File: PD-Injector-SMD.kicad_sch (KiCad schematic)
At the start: 6 parts, among them P1 USB_C_Plug_USB2.0

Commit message: change of form factor and further ECAD work
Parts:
- removed H1: MountingHole, MountingHole:MountingHole_3.2mm_M3_Pad_Via, symbol Mechanical:MountingHole_Pad
- added D1: LED, LED_SMD:LED_0402_1005Metric, symbol Device:LED
- added H2: MountingHole, Eagle_WA-SMSI (rev21a):WA-SMSI_9774005243, symbol Mechanical:MountingHole_Pad
- added R3: 5.1k, Resistor_SMD:R_0402_1005Metric, symbol Device:R
- added TP1, TP2: TestPoint, TestPoint:TestPoint_Pad_D2.0mm, symbol Connector:TestPoint
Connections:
- net GND: now also D1.1 (K), H2.1, TP2.1
- net VBUS: now also TP1.1
- net at USB-C2.A4 (VBUS), USB-C2.B9 (VBUS): now also R3.1
- new net: D1.2 (A), R3.2
- no-connect marks 10 -> 9
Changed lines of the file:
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@@
   (junction (at 175.26 157.48) (diameter 0) (color 0 0 0 0)
   )
+  (junction (at 116.84 57.15) (diameter 0) (color 0 0 0 0)
+  )
   (junction (at 134.62 121.92) (diameter 0) (color 0 0 0 0)
   )
@@
   )
   (junction (at 116.84 134.62) (diameter 0) (color 0 0 0 0)
+  )
+  (junction (at 134.62 119.38) (diameter 0) (color 0 0 0 0)
   )
   (no_connect (at 114.3 69.85))
@@
   (no_connect (at 114.3 144.78))
   (no_connect (at 114.3 142.24))
-  (no_connect (at 114.3 114.3))
   (no_connect (at 83.82 114.3))
   (wire (pts (xy 99.06 97.79) (xy 99.06 99.06))
@@
     (stroke (width 0) (type default) (color 0 0 0 0))
   )
+  (wire (pts (xy 115.57 97.79) (xy 99.06 97.79))
+    (stroke (width 0) (type default) (color 0 0 0 0))
+  )
   (wire (pts (xy 91.44 154.94) (xy 99.06 154.94))
     (stroke (width 0) (type default) (color 0 0 0 0))
@@
     (stroke (width 0) (type default) (color 0 0 0 0))
   )
+  (wire (pts (xy 134.62 114.3) (xy 134.62 119.38))
+    (stroke (width 0) (type default) (color 0 0 0 0))
+  )
   (wire (pts (xy 134.62 121.92) (xy 134.62 119.38))
     (stroke (width 0) (type default) (color 0 0 0 0))
   )
+  (wire (pts (xy 114.3 114.3) (xy 116.84 114.3))
+    (stroke (width 0) (type default) (color 0 0 0 0))
+  )
   (wire (pts (xy 149.86 64.77) (xy 149.86 124.46))
     (stroke (width 0) (type default) (color 0 0 0 0))
@@
   )
   (wire (pts (xy 99.06 154.94) (xy 99.06 156.21))
+    (stroke (width 0) (type default) (color 0 0 0 0))
+  )
+  (wire (pts (xy 132.08 114.3) (xy 134.62 114.3))
     (stroke (width 0) (type default) (color 0 0 0 0))
   )
@@
     (pin "1")
   )
-  (symbol (lib_id "power:GND") (at 173.99 83.82 0) (unit 1)
-    (in_bom yes) (on_board yes)
-    (property "Reference" "#PWR0101" (id 0) (at 173.99 90.17 0)
-      (effects (font (size 1.27 1.27)) hide)
-    )
-    (property "Value" "GND" (id 1) (at 173.99 87.63 0))
-    (property "Footprint" "" (id 2) (at 173.99 83.82 0)
-      (effects (font (size 1.27 1.27)) hide)
-    )
-    (property "Datasheet" "" (id 3) (at 173.99 83.82 0)
+  (symbol (lib_id "power:GND") (at 173.99 97.79 0) (unit 1)
+    (in_bom yes) (on_board yes)
+    (property "Reference" "#PWR0101" (id 0) (at 173.99 104.14 0)
+      (effects (font (size 1.27 1.27)) hide)
+    )
+    (property "Value" "GND" (id 1) (at 173.99 101.6 0))
+    (property "Footprint" "" (id 2) (at 173.99 97.79 0)
+      (effects (font (size 1.27 1.27)) hide)
+    )
+    (property "Datasheet" "" (id 3) (at 173.99 97.79 0)
+      (effects (font (size 1.27 1.27)) hide)
+    )
+    (pin "1")
+  )
+  (symbol (lib_id "Connector:TestPoint") (at 115.57 97.79 270) (unit 1)
+    (in_bom yes) (on_board yes) (fields_autoplaced)
+    (property "Reference" "TP2" (id 0) (at 120.269 96.9553 90)
+      (effects (font (size 1.27 1.27)) (justify left))
+    )
+    (property "Value" "TestPoint" (id 1) (at 120.269 99.4922 90)
+      (effects (font (size 1.27 1.27)) (justify left))
+    )
+    (property "Footprint" "TestPoint:TestPoint_Pad_D2.0mm" (id 2) (at 115.57 102.87 0)
+      (effects (font (size 1.27 1.27)) hide)
+    )
+    (property "Datasheet" "~" (id 3) (at 115.57 102.87 0)
       (effects (font (size 1.27 1.27)) hide)
     )
@@
     (pin "S1")
   )
+  (symbol (lib_id "Device:R") (at 120.65 114.3 90) (unit 1)
+    (in_bom yes) (on_board yes)
+    (property "Reference" "R3" (id 0) (at 120.65 112.268 90))
+    (property "Value" "5.1k" (id 1) (at 120.65 114.3 90))
+    (property "Footprint" "Resistor_SMD:R_0402_1005Metric" (id 2) (at 120.65 116.078 90)
+      (effects (font (size 1.27 1.27)) hide)
+    )
+    (property "Datasheet" "" (id 3) (at 120.65 114.3 0)
+      (effects (font (size 1.27 1.27)) hide)
+    )
+    (pin "1")
+    (pin "2")
+  )
+  (symbol (lib_id "Connector:TestPoint") (at 116.84 57.15 270) (unit 1)
+    (in_bom yes) (on_board yes) (fields_autoplaced)
+    (property "Reference" "TP1" (id 0) (at 121.539 56.3153 90)
+      (effects (font (size 1.27 1.27)) (justify left))
+    )
+    (property "Value" "TestPoint" (id 1) (at 121.539 58.8522 90)
+      (effects (font (size 1.27 1.27)) (justify left))
+    )
+    (property "Footprint" "TestPoint:TestPoint_Pad_D2.0mm" (id 2) (at 116.84 62.23 0)
+      (effects (font (size 1.27 1.27)) hide)
+    )
+    (property "Datasheet" "~" (id 3) (at 116.84 62.23 0)
+      (effects (font (size 1.27 1.27)) hide)
+    )
+    (pin "1")
+  )
+  (symbol (lib_id "Device:LED") (at 128.27 114.3 180) (unit 1)
+    (in_bom yes) (on_board yes) (fields_autoplaced)
+    (property "Reference" "D1" (id 0) (at 129.8702 108.4412 0))
+    (property "Value" "LED" (id 1) (at 129.8702 110.9781 0))
+    (property "Footprint" "LED_SMD:LED_0402_1005Metric" (id 2) (at 128.27 114.3 0)
+      (effects (font (size 1.27 1.27)) hide)
+    )
+    (property "Datasheet" "~" (id 3) (at 128.27 114.3 0)
+      (effects (font (size 1.27 1.27)) hide)
+    )
+    (pin "1")
+    (pin "2")
+  )
   (symbol (lib_id "Connector:USB_C_Receptacle_USB2.0") (at 99.06 72.39 0) (unit 1)
     (in_bom yes) (on_board yes) (fields_autoplaced)
@@
     (pin "S1")
   )
-  (symbol (lib_id "Mechanical:MountingHole_Pad") (at 173.99 81.28 0) (unit 1)
-    (in_bom yes) (on_board yes) (fields_autoplaced)
-    (property "Reference" "H1" (id 0) (at 176.53 80.4453 0)
-      (effects (font (size 1.27 1.27)) (justify left))
-    )
-    (property "Value" "MountingHole" (id 1) (at 176.53 82.9822 0)
-      (effects (font (size 1.27 1.27)) (justify left))
-    )
-    (property "Footprint" "MountingHole:MountingHole_3.2mm_M3_Pad_Via" (id 2) (at 173.99 81.28 0)
-      (effects (font (size 1.27 1.27)) hide)
-    )
-    (property "Datasheet" "~" (id 3) (at 173.99 81.28 0)
+  (symbol (lib_id "Mechanical:MountingHole_Pad") (at 173.99 95.25 0) (unit 1)
+    (in_bom yes) (on_board yes) (fields_autoplaced)
+    (property "Reference" "H2" (id 0) (at 176.53 93.1453 0)
+      (effects (font (size 1.27 1.27)) (justify left))
+    )
+    (property "Value" "MountingHole" (id 1) (at 176.53 95.6822 0)
+      (effects (font (size 1.27 1.27)) (justify left))
+    )
+    (property "Footprint" "Eagle_WA-SMSI (rev21a):WA-SMSI_9774005243" (id 2) (at 173.99 95.25 0)
+      (effects (font (size 1.27 1.27)) hide)
+    )
+    (property "Datasheet" "~" (id 3) (at 173.99 95.25 0)
       (effects (font (size 1.27 1.27)) hide)
     )
@@
       (reference "#PWR0101") (unit 1) (value "GND") (footprint "")
     )
-    (path "/df7c1a03-80dd-4f13-ba65-29ebaf1ac007"
-      (reference "H1") (unit 1) (value "MountingHole") (footprint "MountingHole:MountingHole_3.2mm_M3_Pad_Via")
+    (path "/7d39dc41-6f9d-4f32-b796-4b4569a96c21"
+      (reference "D1") (unit 1) (value "LED") (footprint "LED_SMD:LED_0402_1005Metric")
+    )
+    (path "/f15812da-b2a9-4b21-b46f-2b0bd658c9e0"
+      (reference "H2") (unit 1) (value "MountingHole") (footprint "Eagle_WA-SMSI (rev21a):WA-SMSI_9774005243")
     )
     (path "/b80cf4e8-26ab-421b-9444-ce997b0658b6"
@@
       (reference "R2") (unit 1) (value "5.1k") (footprint "Resistor_SMD:R_0402_1005Metric")
     )
+    (path "/223f621f-8abf-45c8-8712-8588e136e18b"
+      (reference "R3") (unit 1) (value "5.1k") (footprint "Resistor_SMD:R_0402_1005Metric")
+    )
+    (path "/7cf6fa88-c455-48df-afb8-5568c829d338"
+      (reference "TP1") (unit 1) (value "TestPoint") (footprint "TestPoint:TestPoint_Pad_D2.0mm")
+    )
+    (path "/127fd074-fb90-4726-b143-d97766dff79b"
+      (reference "TP2") (unit 1) (value "TestPoint") (footprint "TestPoint:TestPoint_Pad_D2.0mm")
+    )
     (path "/ad170786-1a91-4a0d-94b6-90757b7c7e2b"

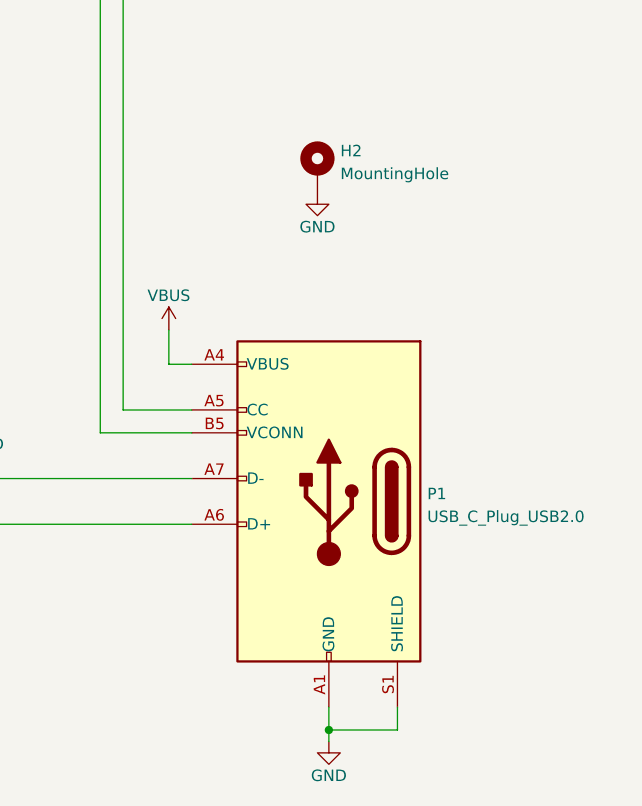
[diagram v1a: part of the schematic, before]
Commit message: finalized PCB work for V0.1
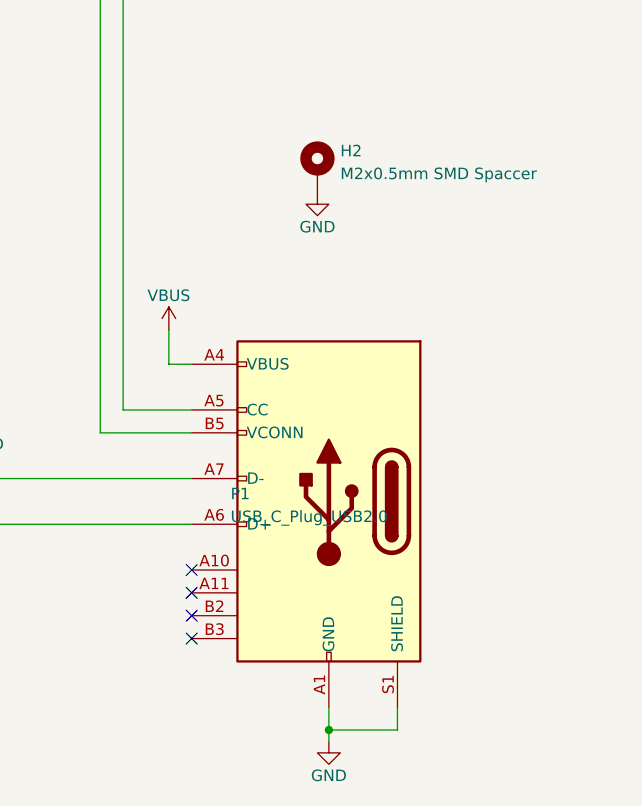
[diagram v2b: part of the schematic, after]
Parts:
- H2: value MountingHole -> M2x0.5mm SMD Spaccer
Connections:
- net GND: no longer P1.A12 (GND), P1.B1 (GND)
- net VBUS: no longer P1.A9 (VBUS), P1.B4 (VBUS)
- no-connect marks 9 -> 13
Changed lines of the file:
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@@
   (no_connect (at 114.3 85.09))
   (no_connect (at 114.3 144.78))
+  (no_connect (at 160.02 139.7))
+  (no_connect (at 160.02 142.24))
+  (no_connect (at 160.02 144.78))
+  (no_connect (at 160.02 147.32))
   (no_connect (at 114.3 142.24))
   (no_connect (at 83.82 114.3))
@@
   (symbol (lib_id "Connector:USB_C_Plug_USB2.0") (at 175.26 132.08 0) (mirror y) (unit 1)
     (in_bom yes) (on_board yes) (fields_autoplaced)
-    (property "Reference" "P1" (id 0) (at 186.182 131.2453 0)
+    (property "Reference" "P1" (id 0) (at 164.338 131.2453 0)
       (effects (font (size 1.27 1.27)) (justify right))
     )
-    (property "Value" "USB_C_Plug_USB2.0" (id 1) (at 186.182 133.7822 0)
+    (property "Value" "USB_C_Plug_USB2.0" (id 1) (at 164.338 133.7822 0)
       (effects (font (size 1.27 1.27)) (justify right))
     )
-    (property "Footprint" "Connector_USB_Extra:USB_C_Plug_UTC009-C12" (id 2) (at 171.45 132.08 0)
-      (effects (font (size 1.27 1.27)) hide)
-    )
-    (property "Datasheet" "https://www.usb.org/sites/default/files/documents/usb_type-c.zip" (id 3) (at 171.45 132.08 0)
+    (property "Footprint" "Connector_USB_Extra:USB_C_Plug_UTC009-C12" (id 2) (at 179.07 132.08 0)
+      (effects (font (size 1.27 1.27)) hide)
+    )
+    (property "Datasheet" "https://www.usb.org/sites/default/files/documents/usb_type-c.zip" (id 3) (at 179.07 132.08 0)
       (effects (font (size 1.27 1.27)) hide)
     )
     (pin "A1")
-    (pin "A12")
+    (pin "B3")
+    (pin "B2")
+    (pin "A11")
+    (pin "A10")
     (pin "A4")
     (pin "A5")
     (pin "A6")
     (pin "A7")
-    (pin "A9")
-    (pin "B1")
     (pin "B12")
-    (pin "B4")
     (pin "B5")
     (pin "B9")
@@
       (effects (font (size 1.27 1.27)) (justify left))
     )
-    (property "Value" "MountingHole" (id 1) (at 176.53 95.6822 0)
+    (property "Value" "M2x0.5mm SMD Spaccer" (id 1) (at 176.53 95.6822 0)
       (effects (font (size 1.27 1.27)) (justify left))
     )
@@
       (effects (font (size 1.27 1.27)) hide)
     )
-    (property "Datasheet" "~" (id 3) (at 173.99 95.25 0)
+    (property "Datasheet" "https://www.we-online.com/katalog/datasheet/9774005243.pdf" (id 3) (at 173.99 95.25 0)
       (effects (font (size 1.27 1.27)) hide)
     )
@@
     )
     (path "/f15812da-b2a9-4b21-b46f-2b0bd658c9e0"
-      (reference "H2") (unit 1) (value "MountingHole") (footprint "Eagle_WA-SMSI (rev21a):WA-SMSI_9774005243")
+      (reference "H2") (unit 1) (value "M2x0.5mm SMD Spaccer") (footprint "Eagle_WA-SMSI (rev21a):WA-SMSI_9774005243")
     )
     (path "/b80cf4e8-26ab-421b-9444-ce997b0658b6"

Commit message: minor schematic clean up
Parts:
- P1: value USB_C_Plug_USB2.0 -> C-UTC09-00
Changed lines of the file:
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@@
       (effects (font (size 1.27 1.27)) (justify right))
     )
-    (property "Value" "USB_C_Plug_USB2.0" (id 1) (at 164.338 133.7822 0)
+    (property "Value" "C-UTC09-00" (id 1) (at 164.338 133.7822 0)
       (effects (font (size 1.27 1.27)) (justify right))
     )
@@
       (effects (font (size 1.27 1.27)) hide)
     )
-    (property "Datasheet" "https://www.usb.org/sites/default/files/documents/usb_type-c.zip" (id 3) (at 179.07 132.08 0)
+    (property "Datasheet" "https://www.solder.party/docs/usb-c-pack/" (id 3) (at 179.07 132.08 0)
       (effects (font (size 1.27 1.27)) hide)
     )
     (pin "A1")
-    (pin "B3")
-    (pin "B2")
+    (pin "A10")
     (pin "A11")
-    (pin "A10")
     (pin "A4")
     (pin "A5")
@@
     (pin "A7")
     (pin "B12")
+    (pin "B2")
+    (pin "B3")
     (pin "B5")
     (pin "B9")
@@
     )
     (path "/b80cf4e8-26ab-421b-9444-ce997b0658b6"
-      (reference "P1") (unit 1) (value "USB_C_Plug_USB2.0") (footprint "Connector_USB_Extra:USB_C_Plug_UTC009-C12")
+      (reference "P1") (unit 1) (value "C-UTC09-00") (footprint "Connector_USB_Extra:USB_C_Plug_UTC009-C12")
     )
     (path "/00000000-0000-0000-0000-000059863ddf"
